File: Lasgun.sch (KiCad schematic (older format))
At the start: 15 parts, among them IC1 ATMEGA328P-A, M1 STM32F042G6, M2 EPSON_FA-20H_CRYSTAL, Q1 Q_NMOS_GSD, U1 74LS08

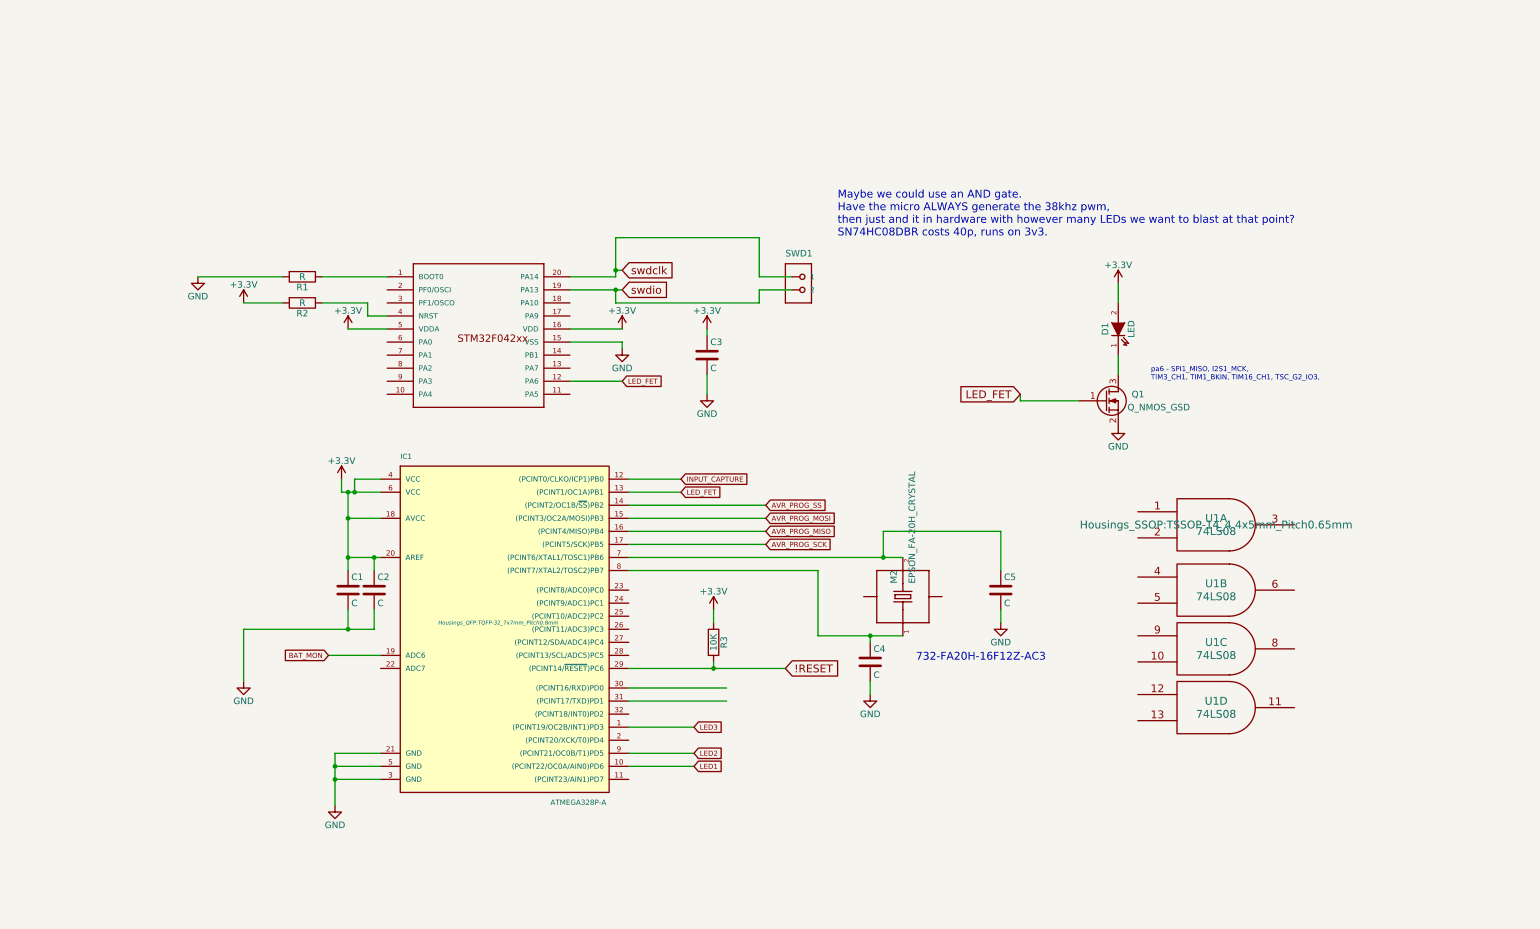
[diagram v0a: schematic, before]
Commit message: Added IR receiver, tried to tidy up Kicad libs
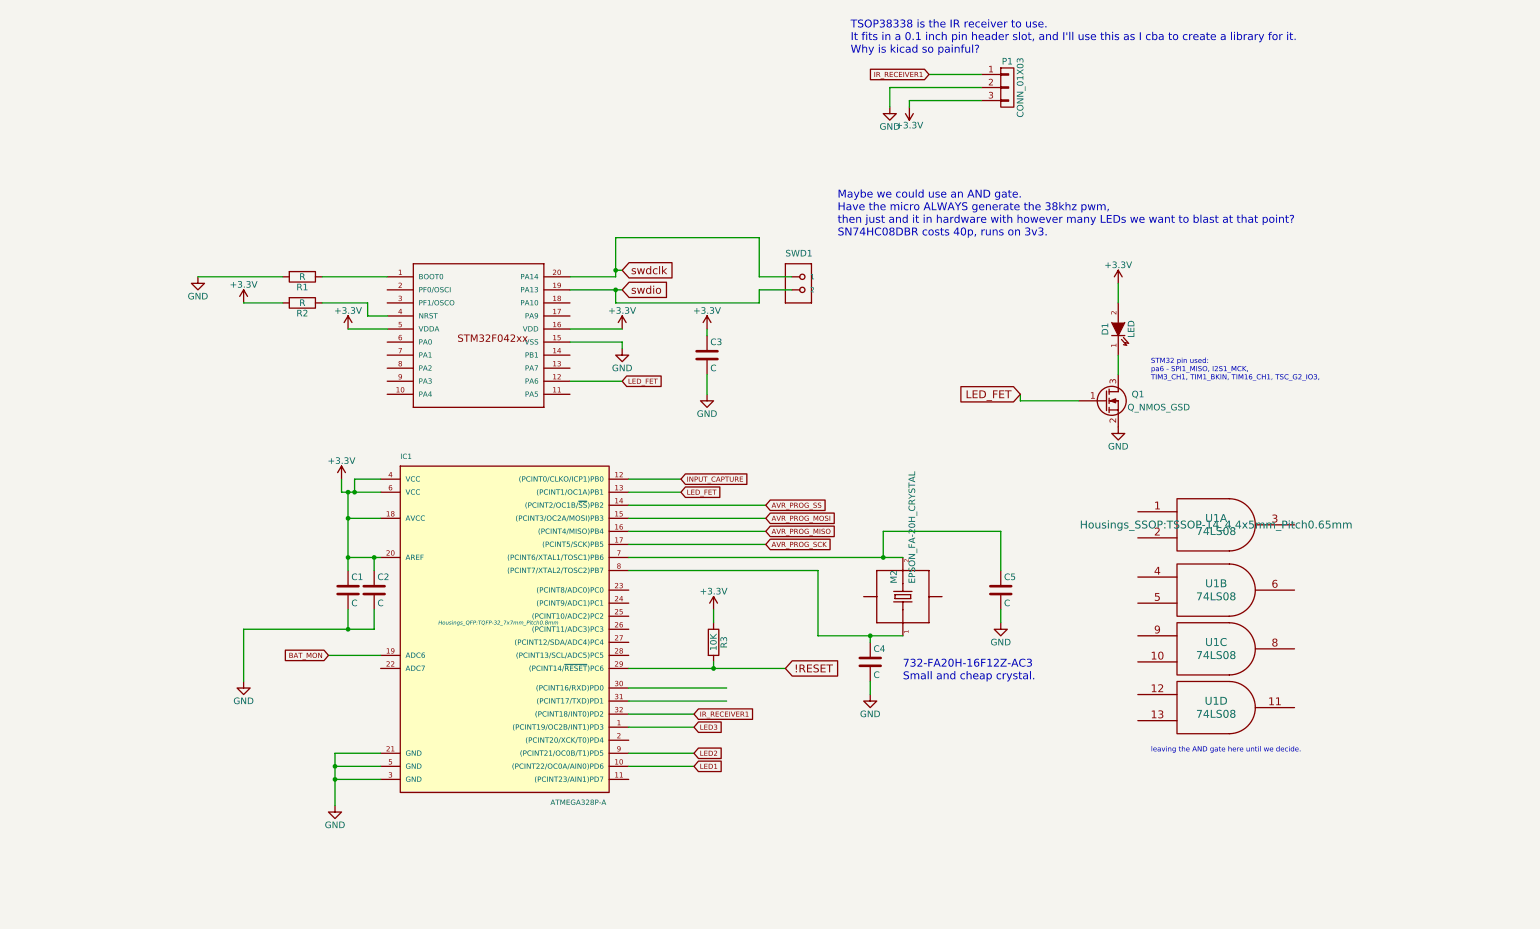
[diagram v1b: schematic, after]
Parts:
- added P1: CONN_01X03, Pin_Headers:Pin_Header_Angled_1x03, symbol CONN_01X03
- U1: footprint (none) -> Housings_SSOP:TSSOP-14_4.4x5mm_Pitch0.65mm
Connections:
- net +3V3: now also P1.3 (P3)
- net GND: now also P1.2 (P2)
- net IR_RECEIVER1: now reaches IC1.32 ((PCINT18/INT0)PD2)
- net IR_RECEIVER1: now also P1.1 (P1)
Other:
- note added: "732-FA20H-16F12Z-AC3\nSmall and cheap crystal.\n"
- note added: "STM32 pin used:\npa6 - SPI1_MISO, I2S1_MCK, \nTIM3_CH1, TIM1_BKIN, TIM16_CH1, TSC_G2_IO3,"
- note added: "TSOP38338 is the IR receiver to use. \nIt fits in a 0.1 inch pin header slot, and I'll use this as I cba to create a library for it. \nWhy is kicad so painful?\n"
- note added: "leaving the AND gate here until we decide.\n"
- note removed: "732-FA20H-16F12Z-AC3"
- note removed: "pa6 - SPI1_MISO, I2S1_MCK, \nTIM3_CH1, TIM1_BKIN, TIM16_CH1, TSC_G2_IO3,"
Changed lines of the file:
@@
 LIBS:STM32F4LQFP144
 LIBS:stm32f072cb
+LIBS:DataStorage
+LIBS:Diodes
+LIBS:Microprocessors
+LIBS:MiscellaneousDevices
+LIBS:Passives
+LIBS:PMOD
+LIBS:PowerComponents
+LIBS:RF_OEM_Parts
+LIBS:Sensors
+LIBS:TransistorParts
+LIBS:Lasgun-cache
 EELAYER 25 0
 EELAYER END
@@
 swdclk
 Text Notes 9200 3350 0    39   ~ 0
-pa6 - SPI1_MISO, I2S1_MCK, \nTIM3_CH1, TIM1_BKIN, TIM16_CH1, TSC_G2_IO3,
+STM32 pin used:\npa6 - SPI1_MISO, I2S1_MCK, \nTIM3_CH1, TIM1_BKIN, TIM16_CH1, TSC_G2_IO3,
 $Comp
 L ATMEGA328P-A IC1
@@
 LED_FET
 $Comp
-L +3.3V #PWR01
+L +3.3V #PWR7
 U 1 1 5637E45F
 P 5150 2950
-F 0 "#PWR01" H 5150 2800 50  0001 C CNN
+F 0 "#PWR7" H 5150 2800 50  0001 C CNN
 F 1 "+3.3V" H 5150 3090 50  0000 C CNN
 F 2 "" H 5150 2950 60  0000 C CNN
@@
 $EndComp
 $Comp
-L +3.3V #PWR02
+L +3.3V #PWR6
 U 1 1 5637E47B
 P 3050 2950
-F 0 "#PWR02" H 3050 2800 50  0001 C CNN
+F 0 "#PWR6" H 3050 2800 50  0001 C CNN
 F 1 "+3.3V" H 3050 3090 50  0000 C CNN
 F 2 "" H 3050 2950 60  0000 C CNN
@@
 $EndComp
 $Comp
-L +3.3V #PWR03
+L +3.3V #PWR5
 U 1 1 5637E4EB
 P 3000 4100
-F 0 "#PWR03" H 3000 3950 50  0001 C CNN
+F 0 "#PWR5" H 3000 3950 50  0001 C CNN
 F 1 "+3.3V" H 3000 4240 50  0000 C CNN
 F 2 "" H 3000 4100 60  0000 C CNN
@@
 $EndComp
 $Comp
-L GND #PWR04
+L GND #PWR4
 U 1 1 5637E5A9
 P 2950 6600
-F 0 "#PWR04" H 2950 6350 50  0001 C CNN
+F 0 "#PWR4" H 2950 6350 50  0001 C CNN
 F 1 "GND" H 2950 6450 50  0000 C CNN
 F 2 "" H 2950 6600 60  0000 C CNN
@@
 $EndComp
 $Comp
-L GND #PWR05
+L GND #PWR8
 U 1 1 5637E6C2
 P 5150 3100
-F 0 "#PWR05" H 5150 2850 50  0001 C CNN
+F 0 "#PWR8" H 5150 2850 50  0001 C CNN
 F 1 "GND" H 5150 2950 50  0000 C CNN
 F 2 "" H 5150 3100 60  0000 C CNN
@@
 $EndComp
 $Comp
-L +3.3V #PWR06
+L +3.3V #PWR2
 U 1 1 5637E81D
 P 2250 2750
-F 0 "#PWR06" H 2250 2600 50  0001 C CNN
+F 0 "#PWR2" H 2250 2600 50  0001 C CNN
 F 1 "+3.3V" H 2250 2890 50  0000 C CNN
 F 2 "" H 2250 2750 60  0000 C CNN
@@
 $EndComp
 $Comp
-L GND #PWR07
+L GND #PWR1
 U 1 1 5637EAF7
 P 1900 2550
-F 0 "#PWR07" H 1900 2300 50  0001 C CNN
+F 0 "#PWR1" H 1900 2300 50  0001 C CNN
 F 1 "GND" H 1900 2400 50  0000 C CNN
 F 2 "" H 1900 2550 60  0000 C CNN
@@
 $EndComp
 $Comp
-L +3.3V #PWR08
+L +3.3V #PWR11
 U 1 1 5637EC9B
 P 5850 5100
-F 0 "#PWR08" H 5850 4950 50  0001 C CNN
+F 0 "#PWR11" H 5850 4950 50  0001 C CNN
 F 1 "+3.3V" H 5850 5240 50  0000 C CNN
 F 2 "" H 5850 5100 60  0000 C CNN
@@
 $EndComp
 $Comp
-L GND #PWR09
+L GND #PWR3
 U 1 1 56380212
 P 2250 5650
-F 0 "#PWR09" H 2250 5400 50  0001 C CNN
+F 0 "#PWR3" H 2250 5400 50  0001 C CNN
 F 1 "GND" H 2250 5500 50  0000 C CNN
 F 2 "" H 2250 5650 60  0000 C CNN
@@
 	1    0    0    -1
 $EndComp
-Text Notes 7400 5500 0    60   ~ 0
-732-FA20H-16F12Z-AC3
+Text Notes 7300 5650 0    60   ~ 0
+732-FA20H-16F12Z-AC3\nSmall and cheap crystal.\n
 $Comp
 L C C4
@@
 	8050 5100 8050 5200
 $Comp
-L GND #PWR010
+L GND #PWR15
 U 1 1 56380940
 P 8050 5200
-F 0 "#PWR010" H 8050 4950 50  0001 C CNN
+F 0 "#PWR15" H 8050 4950 50  0001 C CNN
 F 1 "GND" H 8050 5050 50  0000 C CNN
 F 2 "" H 8050 5200 60  0000 C CNN
@@
 $EndComp
 $Comp
-L GND #PWR011
+L GND #PWR12
 U 1 1 5638095C
 P 7050 5750
-F 0 "#PWR011" H 7050 5500 50  0001 C CNN
+F 0 "#PWR12" H 7050 5500 50  0001 C CNN
 F 1 "GND" H 7050 5600 50  0000 C CNN
 F 2 "" H 7050 5750 60  0000 C CNN
@@
 $EndComp
 $Comp
-L GND #PWR012
+L GND #PWR17
 U 1 1 56380B14
 P 8950 3700
-F 0 "#PWR012" H 8950 3450 50  0001 C CNN
+F 0 "#PWR17" H 8950 3450 50  0001 C CNN
 F 1 "GND" H 8950 3550 50  0000 C CNN
 F 2 "" H 8950 3700 60  0000 C CNN
@@
 $EndComp
 $Comp
-L +3.3V #PWR013
+L +3.3V #PWR16
 U 1 1 56380C22
 P 8950 2600
-F 0 "#PWR013" H 8950 2450 50  0001 C CNN
+F 0 "#PWR16" H 8950 2450 50  0001 C CNN
 F 1 "+3.3V" H 8950 2740 50  0000 C CNN
 F 2 "" H 8950 2600 60  0000 C CNN
@@
 $EndComp
 $Comp
-L +3.3V #PWR014
+L +3.3V #PWR9
 U 1 1 5638162C
 P 5800 2950
-F 0 "#PWR014" H 5800 2800 50  0001 C CNN
+F 0 "#PWR9" H 5800 2800 50  0001 C CNN
 F 1 "+3.3V" H 5800 3090 50  0000 C CNN
 F 2 "" H 5800 2950 60  0000 C CNN
@@
 	5800 3000 5800 2950
 $Comp
-L GND #PWR015
+L GND #PWR10
 U 1 1 56381702
 P 5800 3450
-F 0 "#PWR015" H 5800 3200 50  0001 C CNN
+F 0 "#PWR10" H 5800 3200 50  0001 C CNN
 F 1 "GND" H 5800 3300 50  0000 C CNN
 F 2 "" H 5800 3450 60  0000 C CNN
@@
 F 0 "U1" H 9700 5000 60  0000 C CNN
 F 1 "74LS08" H 9700 4900 60  0000 C CNN
-F 2 "" H 9700 4950 60  0000 C CNN
+F 2 "Housings_SSOP:TSSOP-14_4.4x5mm_Pitch0.65mm" H 9700 4950 60  0001 C CNN
 F 3 "" H 9700 4950 60  0000 C CNN
 	2    9700 4950
@@
 F 0 "U1" H 9700 5450 60  0000 C CNN
 F 1 "74LS08" H 9700 5350 60  0000 C CNN
-F 2 "" H 9700 5400 60  0000 C CNN
+F 2 "Housings_SSOP:TSSOP-14_4.4x5mm_Pitch0.65mm" H 9700 5400 60  0001 C CNN
 F 3 "" H 9700 5400 60  0000 C CNN
 	3    9700 5400
@@
 F 0 "U1" H 9700 5900 60  0000 C CNN
 F 1 "74LS08" H 9700 5800 60  0000 C CNN
-F 2 "" H 9700 5850 60  0000 C CNN
+F 2 "Housings_SSOP:TSSOP-14_4.4x5mm_Pitch0.65mm" H 9700 5850 60  0001 C CNN
 F 3 "" H 9700 5850 60  0000 C CNN
 	4    9700 5850
 	1    0    0    -1
 $EndComp
+Text Notes 6900 850  0    60   ~ 0
+TSOP38338 is the IR receiver to use. \nIt fits in a 0.1 inch pin header slot, and I'll use this as I cba to create a library for it. \nWhy is kicad so painful?\n
+Wire Wire Line
+	7500 1000 7900 1000
+Wire Wire Line
+	7200 1100 7900 1100
+Wire Wire Line
+	7350 1200 7900 1200
+Text GLabel 7500 1000 0    39   Input ~ 0
+IR_RECEIVER1
+Wire Wire Line
+	7200 1100 7200 1250
+Wire Wire Line
+	7350 1200 7350 1250
+$Comp
+L +3.3V #PWR14
+U 1 1 56382F17
+P 7350 1250
+F 0 "#PWR14" H 7350 1100 50  0001 C CNN
+F 1 "+3.3V" H 7350 1390 50  0000 C CNN
+F 2 "" H 7350 1250 60  0000 C CNN
+F 3 "" H 7350 1250 60  0000 C CNN
+	1    7350 1250
+	-1   0    0    1
+$EndComp
+$Comp
+L GND #PWR13
+U 1 1 56382F30
+P 7200 1250
+F 0 "#PWR13" H 7200 1000 50  0001 C CNN
+F 1 "GND" H 7200 1100 50  0000 C CNN
+F 2 "" H 7200 1250 60  0000 C CNN
+F 3 "" H 7200 1250 60  0000 C CNN
+	1    7200 1250
+	1    0    0    -1
+$EndComp
+Text GLabel 5700 5900 2    39   Input ~ 0
+IR_RECEIVER1
+Wire Wire Line
+	5700 5900 5200 5900
+$Comp
+L CONN_01X03 P1
+U 1 1 56384092
+P 8100 1100
+F 0 "P1" H 8100 1300 50  0000 C CNN
+F 1 "CONN_01X03" V 8200 1100 50  0000 C CNN
+F 2 "Pin_Headers:Pin_Header_Angled_1x03" H 8100 1100 60  0001 C CNN
+F 3 "" H 8100 1100 60  0000 C CNN
+	1    8100 1100
+	1    0    0    -1
+$EndComp
+Text Notes 9200 6200 0    39   ~ 0
+leaving the AND gate here until we decide.\n
 $EndSCHEMATC

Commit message: Added datasheets, still working on design
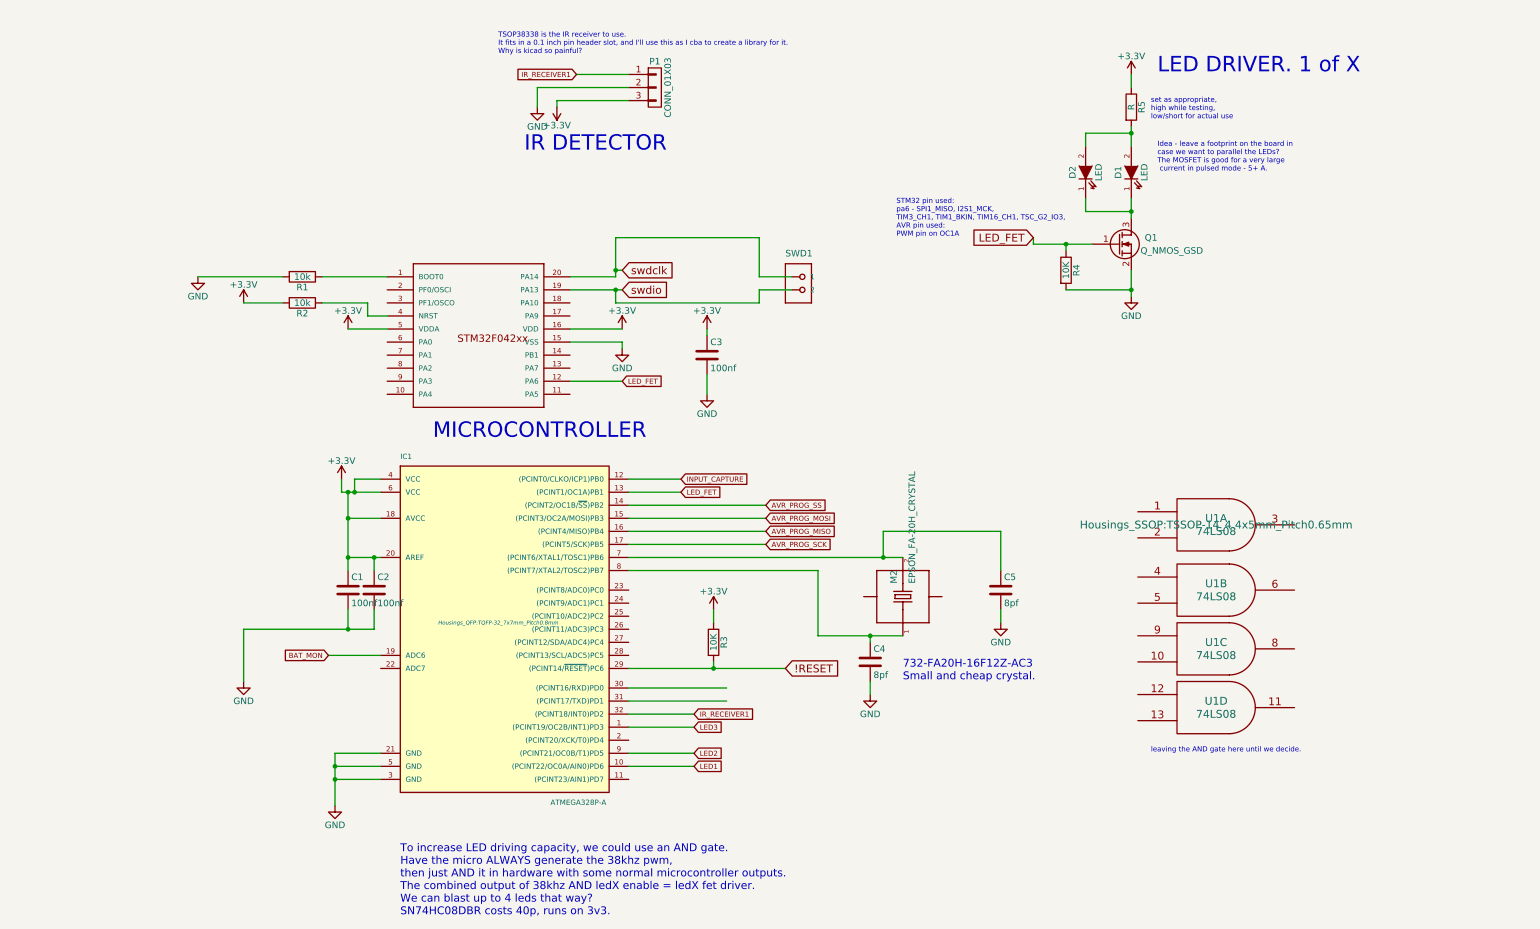
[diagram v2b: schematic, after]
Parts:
- added D2: LED, LEDs:LED-5MM, symbol LED
- added R4: 10K, symbol R
- added R5: R, symbol R
- C1, C2, C3: value C -> 100nf
- C4, C5: value C -> 8pf
- R1, R2: value R -> 10k
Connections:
- net +3V3: now also R5.1; no longer D1.2 (A)
- net GND: now also R4.2
- net LED_FET: now also R4.1
- net at D1.1 (K), Q1.3 (D): now also D2.1 (K)
- new net: D1.2 (A), D2.2 (A), R5.2
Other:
- note added: "IR DETECTOR"
- note added: "Idea - leave a footprint on the board in \ncase we want to parallel the LEDs?\nThe MOSFET is good for a very large\n current in pulsed mode - 5+ A."
- note added: "LED DRIVER. 1 of X\n"
- note added: "MICROCONTROLLER"
- note added: "STM32 pin used:\npa6 - SPI1_MISO, I2S1_MCK, \nTIM3_CH1, TIM1_BKIN, TIM16_CH1, TSC_G2_IO3,\nAVR pin used:\nPWM pin on OC1A"
- note added: "To increase LED driving capacity, we could use an AND gate. \nHave the micro ALWAYS generate the 38khz pwm, \nthen just AND it in hardware with some normal microcontroller outputs. \nThe combined output of 38khz AND ledX enable = ledX fet driver.\nWe can blast up to 4 leds that way? \nSN74HC08DBR costs 40p, runs on 3v3."
- note added: "set as appropriate, \nhigh while testing, \nlow/short for actual use"
- note removed: "Maybe we could use an AND gate. \nHave the micro ALWAYS generate the 38khz pwm, \nthen just and it in hardware with however many LEDs we want to blast at that point? \nSN74HC08DBR costs 40p, runs on 3v3."
- note removed: "STM32 pin used:\npa6 - SPI1_MISO, I2S1_MCK, \nTIM3_CH1, TIM1_BKIN, TIM16_CH1, TSC_G2_IO3,"
- moved on the sheet: D1, P1, Q1

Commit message: Refined design, added parts, started to plan board
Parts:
- removed SWD1: CON_HEADER_1X02-PTH, Wire_Pads:SolderWirePad_2x_0-8mmDrill, symbol CON_HEADER_1X02-PTH
- removed U1: 74LS08, Housings_SSOP:TSSOP-14_4.4x5mm_Pitch0.65mm, symbol 74LS08
- added BATSIG1: BAT_SIG, symbol CONN_01X03
- added CON1: AVR-ISP-6, AVR-ISP-6, symbol AVR-ISP-6
- added P2: CONN_01X03, Pin_Headers:Pin_Header_Angled_1x03, symbol CONN_01X03
- added POW2: R, Resistors_SMD:R_2010_HandSoldering, symbol R
- added R5: 1k, Resistors_SMD:R_0603, symbol R
- added R6: 100, Resistors_SMD:R_0603, symbol R
- POW1: renamed from R5; footprint (none) -> Resistors_SMD:R_2010_HandSoldering
- R4: footprint (none) -> Resistors_SMD:R_0603
- renumbered C4 to cy1, C5 to cy2
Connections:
- net !RESET is gone; now on net ~RESET: IC1.29 ((PCINT14/~RESET~)PC6), R3.2
- net AVR_PROG_SS is gone; now on net LED3: IC1.14 ((PCINT2/OC1B/~SS~)PB2)
- net swdclk is gone; now on net AVR_PROG_SCK: M1.20 (PA14)
- net swdio is gone; now on net AVR_PROG_MISO: M1.19 (PA13)
- net +3V3: now also BATSIG1.2 (P2), CON1.2, P2.3 (P3); no longer POW1.1, R2.2
- net AVR_PROG_MISO: now also CON1.1
- net AVR_PROG_MOSI: now also CON1.4
- net AVR_PROG_SCK: now also CON1.3
- net BAT_MON: now also M1.6 (PA0), R2.1, R5.2
- net GND: now also BATSIG1.3 (P3), CON1.6, P2.2 (P2), R5.1
- net INPUT_CAPTURE: now also M1.7 (PA1), BATSIG1.1 (P1)
- net LED3: no longer IC1.1 ((PCINT19/OC2B/INT1)PD3)
- net LED_FET: now also R6.2; no longer Q1.1 (G), R4.1
- net ~RESET: now reaches M1.4 (NRST)
- net ~RESET: now also CON1.5; no longer R2.1
- net MICRO_TXOUT: now reaches M1.8 (PA2)
- net MICRO_TXOUT: now also IC1.31 ((PCINT17/TXD)PD1)
- net MICRO_RXIN: now reaches M1.9 (PA3)
- net MICRO_RXIN: now also IC1.30 ((PCINT16/RXD)PD0)
- net at D1.2 (A), D2.2 (A), POW1.2: now also POW2.2
- new net: Q1.1 (G), R4.1, R6.1
- new net +BATT: POW1.1, POW2.1, R2.2
- new net IR_RECEIVER2: P2.1 (P1)
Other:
- note added: "11:1 voltage divider \nCan monitor battery voltage here."
- note added: "Always put positive voltage connector in middle\nMeans you can't plug it in the wrong way round\nand then kill things!"
- note added: "MICROCONTROLLER\nSTM32 OR ATMEGA328"
- note added: "PA3, PA4 - UART2_TX, RX"
- note added: "Reuse the AVR connector for programming the STM32\navr_sck = swdclk\navr_miso = swdio"
- note added: "TODO: Need to add the PFET to kill off power to the external flight control board"
- note added: "pa0 - adc_in0"
- note added: "pa1 - tim2_ch2"
- note removed: "MICROCONTROLLER"
- note removed: "To increase LED driving capacity, we could use an AND gate. \nHave the micro ALWAYS generate the 38khz pwm, \nthen just AND it in hardware with some normal microcontroller outputs. \nThe combined output of 38khz AND ledX enable = ledX fet driver.\nWe can blast up to 4 leds that way? \nSN74HC08DBR costs 40p, runs on 3v3."
- note removed: "leaving the AND gate here until we decide.\n"
- moved on the sheet: POW1
